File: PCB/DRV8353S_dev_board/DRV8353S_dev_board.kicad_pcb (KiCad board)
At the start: 4 copper layers, 100 x 85 mm, 144 parts, among them Q1 BSS84, Q2 CSD19502, Q3 CSD19502, Q4 CSD19502, Q5 CSD19502, Q6 CSD19502, Q7 CSD19502, U1 ECS-33B, U2 STM32F042K4Ux, U3 MIC5283-3.3ML-TR, U4 MIC5283-5.0ML-TR, U5 DRV8353SM

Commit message: Changed MCU due to low digikey stock. Also new routing
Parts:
- removed C1, C6: 12pF, Capacitor_SMD:C_0603_1608Metric
- removed C14, C15, C16: 1uF, Capacitor_SMD:C_0805_2012Metric
- removed C17, C18, C19, C20, C21, C22, C23, C35: 22nF, Capacitor_SMD:C_0603_1608Metric
- removed G***: LOGO, DRV8353S_dev_board:school_logo
- removed R11, R12, R13, R14, R15, R16, R17, R18, R19: 0, Resistor_SMD:R_0603_1608Metric
- removed R26, R27, R28, R32, R33, R34: 2.2k, Resistor_SMD:R_0603_1608Metric
- removed R29, R30, R31, R56: 330, Resistor_SMD:R_0603_1608Metric
- removed SPEED PWM: THT, DRV8353S_dev_board:keystone_5001
- removed U1: ECS-33B, DRV8353S_dev_board:ECS-33B
- removed U2: STM32F042K4Ux, Package_DFN_QFN:QFN-32-1EP_5x5mm_P0.5mm_EP3.45x3.45mm
- moved SWD 87.2 mm to (135.8, 149.8), turned to 90 degrees
- moved D4 85.0 mm to (138.6, 146.6), turned to 270 degrees
- moved D5 30.1 mm to (31.6, 120.9)
- moved EXTERNAL UART 30.1 mm to (27.9, 120.8)
- moved L1 23.4 mm to (65.5, 154.0)
- moved L2 23.4 mm to (67.1, 154.0)
- moved L3 23.4 mm to (68.8, 154.0)
- moved Q1 23.4 mm to (73.0, 150.9)
- moved R8 23.4 mm to (68.8, 150.9)
- moved L4 23.4 mm to (70.4, 154.0)
- moved R35 23.4 mm to (70.4, 150.9)
- moved R6 23.4 mm to (65.5, 150.9)
- moved R7 23.4 mm to (67.1, 150.9)
- moved FASTER 20.4 mm to (110.1, 152.8)
- moved R2 20.4 mm to (117.3, 148.8)
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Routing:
- net +5V: track 206.3 -> 0.00 mm, vias 8 -> 5
- net /~RESET_PB: track 79.1 -> 0.00 mm, vias 2 -> 0
- net /DIRECTION_DIP: track 71.3 -> 0.00 mm
- net /~SPEED_UP_PB: track 63.7 -> 0.00 mm
- net /~BRAKE: track 60.6 -> 0.00 mm, vias 2 -> 0
- net /~SPEED_DOWN_PB: track 57.7 -> 0.00 mm
- net /DIRECTION: track 54.6 -> 0.00 mm, vias 2 -> 0
- net /~BRAKE_PB: track 52.4 -> 0.00 mm
- net /I_PHASE_C: track 48.2 -> 0.00 mm, vias 2 -> 0
- net /I_PHASE_B: track 42.2 -> 0.00 mm, vias 2 -> 0
- net /~DRV8353_FAULT: track 40.1 -> 0.00 mm, vias 2 -> 0
- net /MOT_TEMP: track 76.1 -> 36.7 mm
- net /SPEED_PWM: track 38.6 -> 0.00 mm, vias 2 -> 0
- net /EXT_UART_RX: track 35.4 -> 0.00 mm
- net /EXT_UART_TX: track 34.2 -> 0.00 mm
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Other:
- board size 100 x 85 mm -> 100 x 67 mm
- board text removed: "DRV8353SM Evaluation Board Francis Walsh 2021"

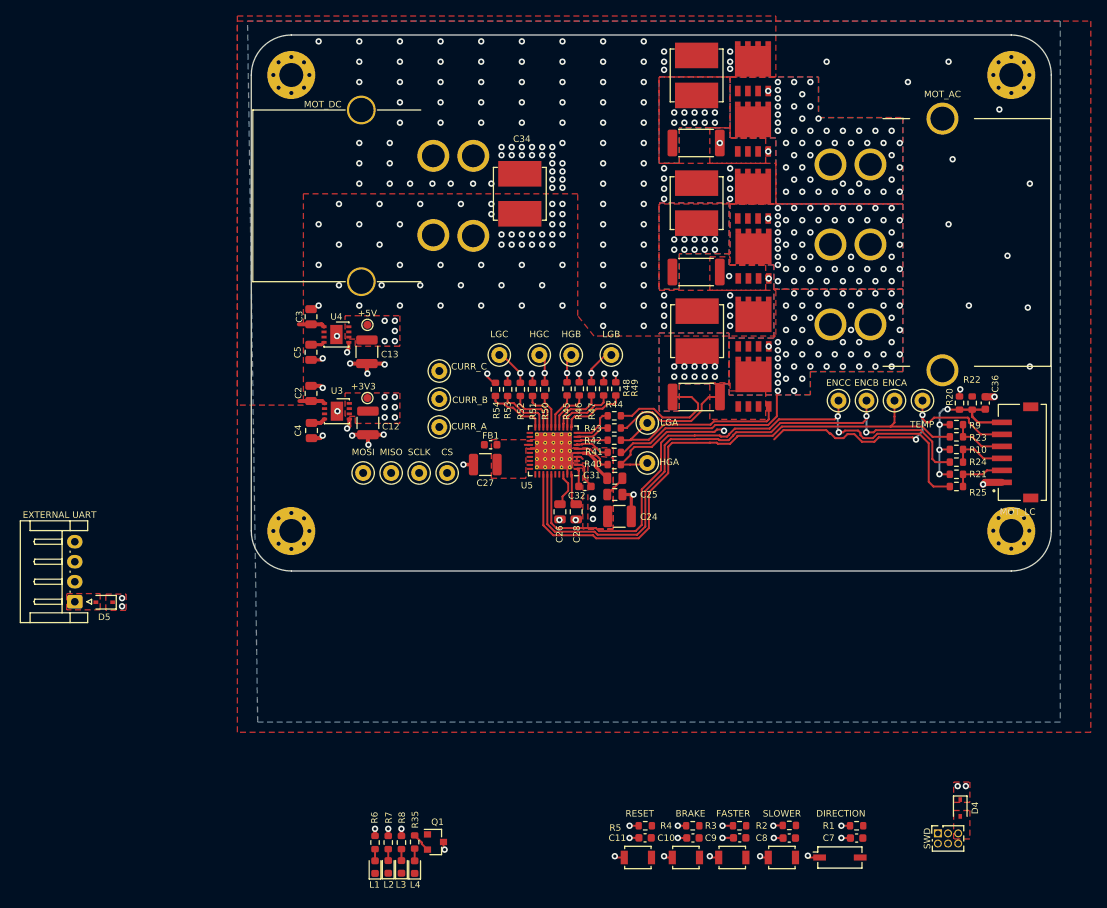
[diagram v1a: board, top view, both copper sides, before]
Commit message: updated MCU due to low digi stock. This was bad routing to get new MCU pinout
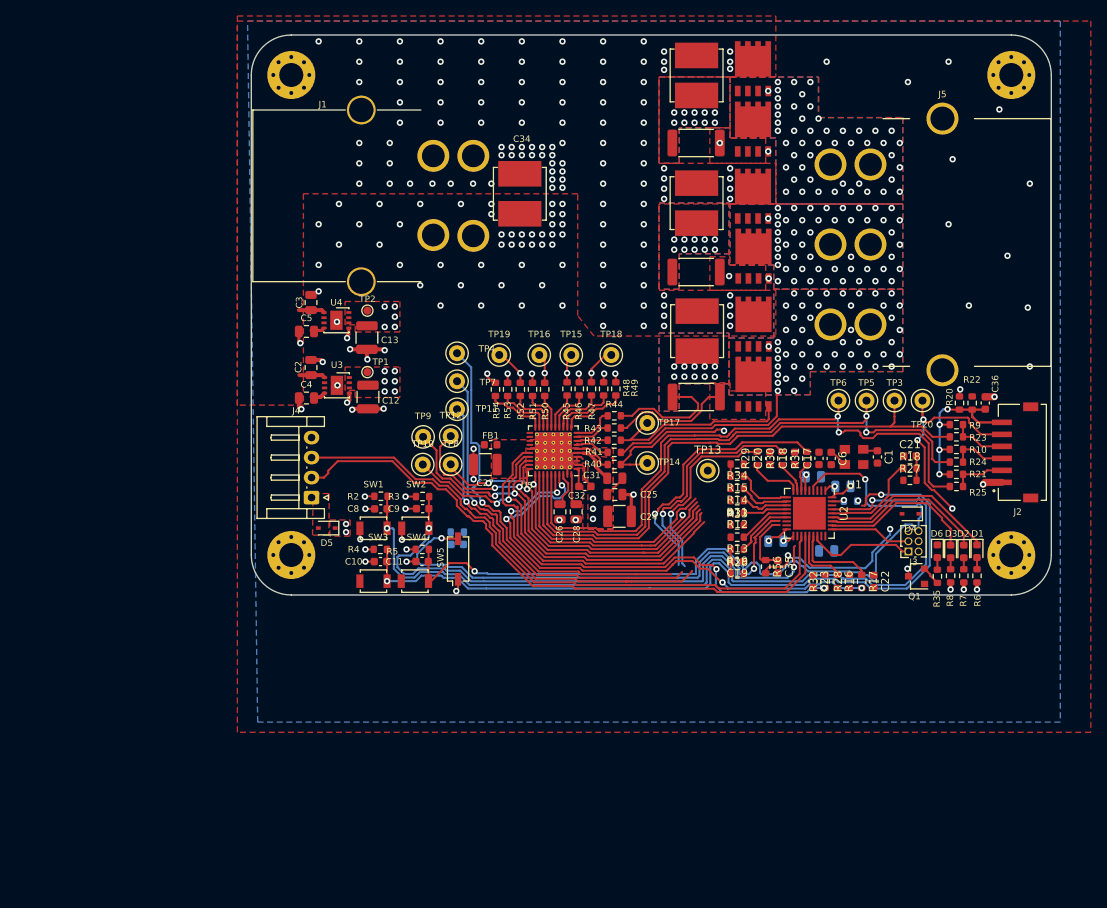
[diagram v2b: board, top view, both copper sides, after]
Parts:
- removed +3V3, +5V: SMD, TestPoint:TestPoint_Pad_D1.0mm
- removed BRAKE, RESET: B3U, Button_Switch_SMD:SW_SPST_B3U-1000P
- removed DIRECTION: DIP, Button_Switch_SMD:SW_DIP_SPSTx01_Slide_Copal_CHS-01A_W5.08mm_P1.27mm_JPin
- removed EXTERNAL UART: EXT_CMD, Connector_JST:JST_EH_S4B-EH_1x04_P2.50mm_Horizontal
- removed MISO, MOSI, SCLK: THT, DRV8353S_dev_board:keystone_5001
- added C1: 12pF, Capacitor_SMD:C_0603_1608Metric, F.Cu at (128.3, 102.7)
- added C14: 1uF, Capacitor_SMD:C_0805_2012Metric, B.Cu at (121.9, 114.5)
- added C15: 1uF, Capacitor_SMD:C_0805_2012Metric, B.Cu at (124.0, 106.4)
- added C16: 1uF, Capacitor_SMD:C_0805_2012Metric, B.Cu at (115.6, 113.3)
- added C17: 22nF, Capacitor_SMD:C_0603_1608Metric, F.Cu at (121.0, 102.9)
- added C18: 22nF, Capacitor_SMD:C_0603_1608Metric, F.Cu at (117.9, 102.9)
- added C19: 22nF, Capacitor_SMD:C_0603_1608Metric, F.Cu at (110.7, 115.8)
- added C20: 22nF, Capacitor_SMD:C_0603_1608Metric, F.Cu at (114.8, 102.9)
- added C21: 22nF, Capacitor_SMD:C_0603_1608Metric, F.Cu at (132.3, 102.6)
- added C22: 22nF, Capacitor_SMD:C_0603_1608Metric, F.Cu at (127.8, 118.3)
- added C23: 22nF, Capacitor_SMD:C_0603_1608Metric, F.Cu at (120.2, 118.3)
- added C35: 22nF, Capacitor_SMD:C_0603_1608Metric, F.Cu at (115.8, 116.5)
- added C37: 1uF, Capacitor_SMD:C_0805_2012Metric, B.Cu at (120.3, 105.2)
- added C6: 12pF, Capacitor_SMD:C_0603_1608Metric, F.Cu at (122.5, 102.9)
- added J4: EXT_CMD, Connector_JST:JST_EH_S4B-EH_1x04_P2.50mm_Horizontal, F.Cu at (57.5, 107.8)
- added R11: 0, Resistor_SMD:R_0603_1608Metric, F.Cu at (110.7, 108.2)
- added R12: 0, Resistor_SMD:R_0603_1608Metric, F.Cu at (110.7, 109.7)
- added R13: 0, Resistor_SMD:R_0603_1608Metric, F.Cu at (110.7, 112.8)
- added R14: 0, Resistor_SMD:R_0603_1608Metric, F.Cu at (110.7, 106.7)
- added R15: 0, Resistor_SMD:R_0603_1608Metric, F.Cu at (110.7, 105.2)
- added R16: 0, Resistor_SMD:R_0603_1608Metric, F.Cu at (123.3, 118.3)
- added R17: 0, Resistor_SMD:R_0603_1608Metric, F.Cu at (126.3, 118.3)
- added R18: 0, Resistor_SMD:R_0603_1608Metric, F.Cu at (132.3, 104.1)
- added R19: 0, Resistor_SMD:R_0603_1608Metric, F.Cu at (110.7, 114.3)
- added R26: 2.2k, Resistor_SMD:R_0603_1608Metric, F.Cu at (110.7, 117.3)
- added R27: 2.2k, Resistor_SMD:R_0603_1608Metric, F.Cu at (132.3, 105.7)
- added R28: 2.2k, Resistor_SMD:R_0603_1608Metric, F.Cu at (124.8, 118.3)
- added R29: 330, Resistor_SMD:R_0603_1608Metric, F.Cu at (113.2, 102.9)
- added R30: 330, Resistor_SMD:R_0603_1608Metric, F.Cu at (116.3, 102.9)
- added R31: 330, Resistor_SMD:R_0603_1608Metric, F.Cu at (119.4, 102.9)
- added R32: 2.2k, Resistor_SMD:R_0603_1608Metric, F.Cu at (121.7, 118.3)
- added R33: 2.2k, Resistor_SMD:R_0603_1608Metric, F.Cu at (110.7, 111.3)
- added R34: 2.2k, Resistor_SMD:R_0603_1608Metric, F.Cu at (110.7, 103.6)
- added R36: 2.2k, Resistor_SMD:R_0603_1608Metric, B.Cu at (124.9, 108.3)
- added R56: 330, Resistor_SMD:R_0603_1608Metric, F.Cu at (114.3, 116.5)
- added SW3: B3U, Button_Switch_SMD:SW_SPST_B3U-1000P, F.Cu at (65.3, 118.3)
- added SW4: B3U, Button_Switch_SMD:SW_SPST_B3U-1000P, F.Cu at (70.4, 118.3)
- added SW5: DIP, Button_Switch_SMD:SW_DIP_SPSTx01_Slide_Copal_CHS-01A_W5.08mm_P1.27mm_JPin, F.Cu at (75.8, 115.5)
- added TP1: SMD, TestPoint:TestPoint_Pad_D1.0mm, F.Cu at (64.5, 92.1)
- added TP10: THT, DRV8353S_dev_board:keystone_5001, F.Cu at (71.4, 103.7)
- added TP12: THT, DRV8353S_dev_board:keystone_5001, F.Cu at (74.9, 100.1)
- added TP13: THT, DRV8353S_dev_board:keystone_5001, F.Cu at (107.1, 104.5)
- added TP2: SMD, TestPoint:TestPoint_Pad_D1.0mm, F.Cu at (64.5, 84.5)
- added TP9: THT, DRV8353S_dev_board:keystone_5001, F.Cu at (71.5, 100.2)
- added U1: ECS-33B, DRV8353S_dev_board:ECS-33B, F.Cu at (125.3, 102.7)
- added U2: STM32F103TBUx, Package_DFN_QFN:QFN-36-1EP_6x6mm_P0.5mm_EP4.1x4.1mm, F.Cu at (119.8, 109.8)
- C7, R1: moved to B.Cu
- moved D1 85.0 mm to (140.7, 114.5), turned to 270 degrees
- moved R6 82.3 mm to (140.7, 117.6), turned to 270 degrees
- moved D2 82.0 mm to (139.1, 114.6), turned to 270 degrees
- moved R7 79.3 mm to (139.1, 117.6), turned to 270 degrees
- moved D3 79.2 mm to (137.4, 114.6), turned to 270 degrees
- moved D6 76.3 mm to (135.8, 114.5), turned to 270 degrees
- moved R8 76.3 mm to (137.4, 117.6), turned to 270 degrees
- moved R35 73.3 mm to (135.8, 117.7), turned to 270 degrees
- moved Q1 68.7 mm to (133.2, 117.7), turned to 180 degrees
- moved R2 65.6 mm to (66.2, 107.7)
- moved SW1 65.6 mm to (65.3, 111.7)
- moved C8 65.6 mm to (66.2, 109.2)
- moved C7 62.0 mm to (75.8, 113.7), turned to 180 degrees
- moved R1 62.0 mm to (75.8, 112.1), turned to 0 degrees
- moved SW2 57.1 mm to (70.5, 111.7)
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- renumbered L1 to D1, L2 to D2, L3 to D3, L4 to D6, MOT_DC to J1, MOT_LC to J2, SWD to J3, MOT_AC to J5, SLOWER to SW1, FASTER to SW2, CURR_A to TP11, HGA to TP14, HGB to TP15, HGC to TP16, LGA to TP17, LGB to TP18, LGC to TP19, TEMP to TP20, ENCA to TP3, CURR_C to TP4, ENCB to TP5, ENCC to TP6, CURR_B to TP7, CS to TP8
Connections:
- FB1 pad 2: Net-(FB1-Pad2) -> +3V3
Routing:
- net /~SPEED_UP_PB: track 0.00 -> 104.6 mm, vias 0 -> 2
- net /~RESET_PB: track 0.00 -> 100.1 mm, vias 0 -> 2
- net /~BRAKE_PB: track 0.00 -> 97.1 mm, vias 0 -> 2
- net /I_PHASE_C: track 0.00 -> 80.3 mm, vias 0 -> 2
- net /EXT_UART_RX: track 0.00 -> 77.6 mm
- net /I_PHASE_B: track 0.00 -> 76.3 mm, vias 0 -> 2
- net /EXT_UART_TX: track 0.00 -> 75.1 mm
- net /I_PHASE_A: track 0.00 -> 70.4 mm, vias 0 -> 2
- net /~SPEED_DOWN_PB: track 0.00 -> 69.9 mm, vias 0 -> 2
- net /~BRAKE: track 0.00 -> 62.5 mm, vias 0 -> 4
- net /DIRECTION_DIP: track 0.00 -> 61.9 mm, vias 0 -> 2
- net /DIRECTION: track 0.00 -> 56.6 mm, vias 0 -> 4
- net /MOSI: track 0.00 -> 53.6 mm, vias 0 -> 2
- net /MISO: track 0.00 -> 52.5 mm, vias 0 -> 3
- net /SCLK: track 0.00 -> 51.0 mm, vias 0 -> 2
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- removed copper zone on F.Cu, net Net-(D4-Pad2)
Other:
- board size 100 x 67 mm -> 100 x 70 mm

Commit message: Good routing
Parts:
- C14: moved to F.Cu
- D4: moved to B.Cu
- moved D4 3.52 mm to (129.7, 112.1), turned to 0 degrees
- moved C21 1.27 mm to (132.3, 103.9)
- moved R27 1.27 mm to (132.3, 106.9)
- moved R18 1.27 mm to (132.3, 105.4)
- moved C14 0.92 mm to (122.8, 114.2)
- moved TP11 0.84 mm to (74.9, 96.7)
- moved TP4 0.84 mm to (74.9, 89.7)
- moved TP7 0.84 mm to (74.9, 93.2)
- moved C9 0.06 mm to (71.4, 109.2)
- moved R3 0.06 mm to (71.3, 107.7)
- moved SW2 0.06 mm to (70.4, 111.7)
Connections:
- U2 pad 32: /DRV8353_EN_JMP -> /~BRAKE_PB
- U2 pad 34: /~BRAKE_PB -> /DRV8353_EN_JMP
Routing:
- net /~RESET_PB: track 100.1 -> 7.76 mm, vias 2 -> 1
- net /~SPEED_DOWN_PB: track 69.9 -> 5.96 mm, vias 2 -> 1
- net /DIRECTION_DIP: track 61.9 -> 2.27 mm, vias 2 -> 1
- net /DRV8353_EN: track 31.0 -> 82.1 mm
- net /~SPEED_UP_PB: track 104.6 -> 70.3 mm, vias 2 -> 1
- net /~BRAKE_PB: track 97.1 -> 67.5 mm, vias 2 -> 1
- net /I_PHASE_C: track 80.3 -> 93.5 mm, vias 2 -> 4
- net /I_PHASE_B: track 76.3 -> 87.4 mm, vias 2 -> 4
- net /I_PHASE_A: track 70.4 -> 81.3 mm, vias 2 -> 4
- net /SPEED_PWM: track 31.1 -> 41.3 mm
- net /XTAL_IN: track 1.84 -> 10.6 mm
- net /MOT_TEMP: track 57.0 -> 64.8 mm, vias 5 -> 1
- net /~DRV8353_CS: track 44.5 -> 52.1 mm
- net /SCLK: track 51.0 -> 58.2 mm
- net GND: track 181.6 -> 187.6 mm, vias 152 -> 159
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
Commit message: As ordered PCB
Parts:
- removed SW1: B3U, Button_Switch_SMD:SW_SPST_B3U-1000P
- added G***: LOGO, DRV8353S_dev_board:school_logo, F.Cu at (129.0, 56.6)
- added SUP: B3U, Button_Switch_SMD:SW_SPST_B3U-1000P, F.Cu at (65.3, 111.7)
- C7, R1: moved to F.Cu
- EXT UART: renamed from J4
- MOT DIR: renamed from SW5
- moved C7 4.15 mm to (75.7, 109.5)
- moved R1 1.08 mm to (75.7, 111.1)
- moved D5 0.25 mm to (59.4, 111.9)
- moved C4 0.25 mm to (56.6, 95.4)
- moved C5 0.25 mm to (56.6, 87.1)
- renumbered TP1 to +3V3, TP2 to +5V0, SW3 to BRAKE, TP8 to CS, TP3 to ENCA, TP5 to ENCB, TP6 to ENCC, J2 to ENCODER, TP14 to GHA, TP15 to GHB, TP16 to GHC, TP17 to GLA, TP18 to GLB, TP19 to GLC, J5 to HC_AC, J1 to HC_DC, TP11 to I_A, TP7 to I_B, TP4 to I_C, D6 to L1, D3 to L2, D2 to L3, D1 to L4, TP10 to MISO, TP9 to MOSI, SW4 to RESET, TP12 to SCLK, SW2 to SDOW, J3 to SWD, TP20 to TEMP
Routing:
- net +5V: track 0.00 -> 175.3 mm, vias 5 -> 6
- net /~RESET_PB: track 7.76 -> 109.3 mm, vias 1 -> 4
- net /~SPEED_DOWN_PB: track 5.96 -> 61.5 mm, vias 1 -> 2
- net /DIRECTION_DIP: track 2.27 -> 56.9 mm, vias 1 -> 2
- net /~SPEED_UP_PB: track 70.3 -> 116.4 mm, vias 1 -> 2
- net /~BRAKE_PB: track 67.5 -> 104.6 mm, vias 1 -> 2
- net /~DRV8353_FAULT: track 46.5 -> 75.9 mm, vias 0 -> 2
- net GND: track 187.6 -> 207.9 mm, vias 159 -> 181
- net +3V3: track 29.2 -> 37.8 mm, vias 21 -> 28
- net /I_PHASE_C: track 93.5 -> 88.1 mm
- net /I_PHASE_B: track 87.4 -> 82.9 mm
- net /DRV8353_EN: track 82.1 -> 86.1 mm, vias 2 -> 4
- net /I_PHASE_A: track 81.3 -> 77.4 mm
- net /~BRAKE: track 60.4 -> 63.5 mm
- net /DIRECTION: track 56.0 -> 59.0 mm
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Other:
- board text added: "DRV8353SM Evaluation Board Designed by: Francis Walsh March, 2021"
